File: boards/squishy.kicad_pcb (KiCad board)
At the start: 4 copper layers, 82 x 56.5 mm, 161 parts, among them J1 USB3_Micro_B_Amphenol, J2 Conn_02x26_Top_Bottom, U1 FT600Q-B-T, U10 THVD1451, U11 THVD1451, U12 THVD1451, U13 THVD1451, U14 THVD1451, U15 THVD1451, U16 THVD1451, U17 THVD1451, U18 THVD1451, U19 THVD1451, U2 ICE40HX8K-BG121, U20 THVD1451, U21 TXB0106, U22 TXB0106, U23 TXB0106, U24 TXB0106, U25 TXB0106, U26 TXB0106, U3 THVD1451, U4 THVD1451, U5 THVD1451, U6 THVD1451, U7 THVD1451, U8 THVD1451, U9 THVD1451

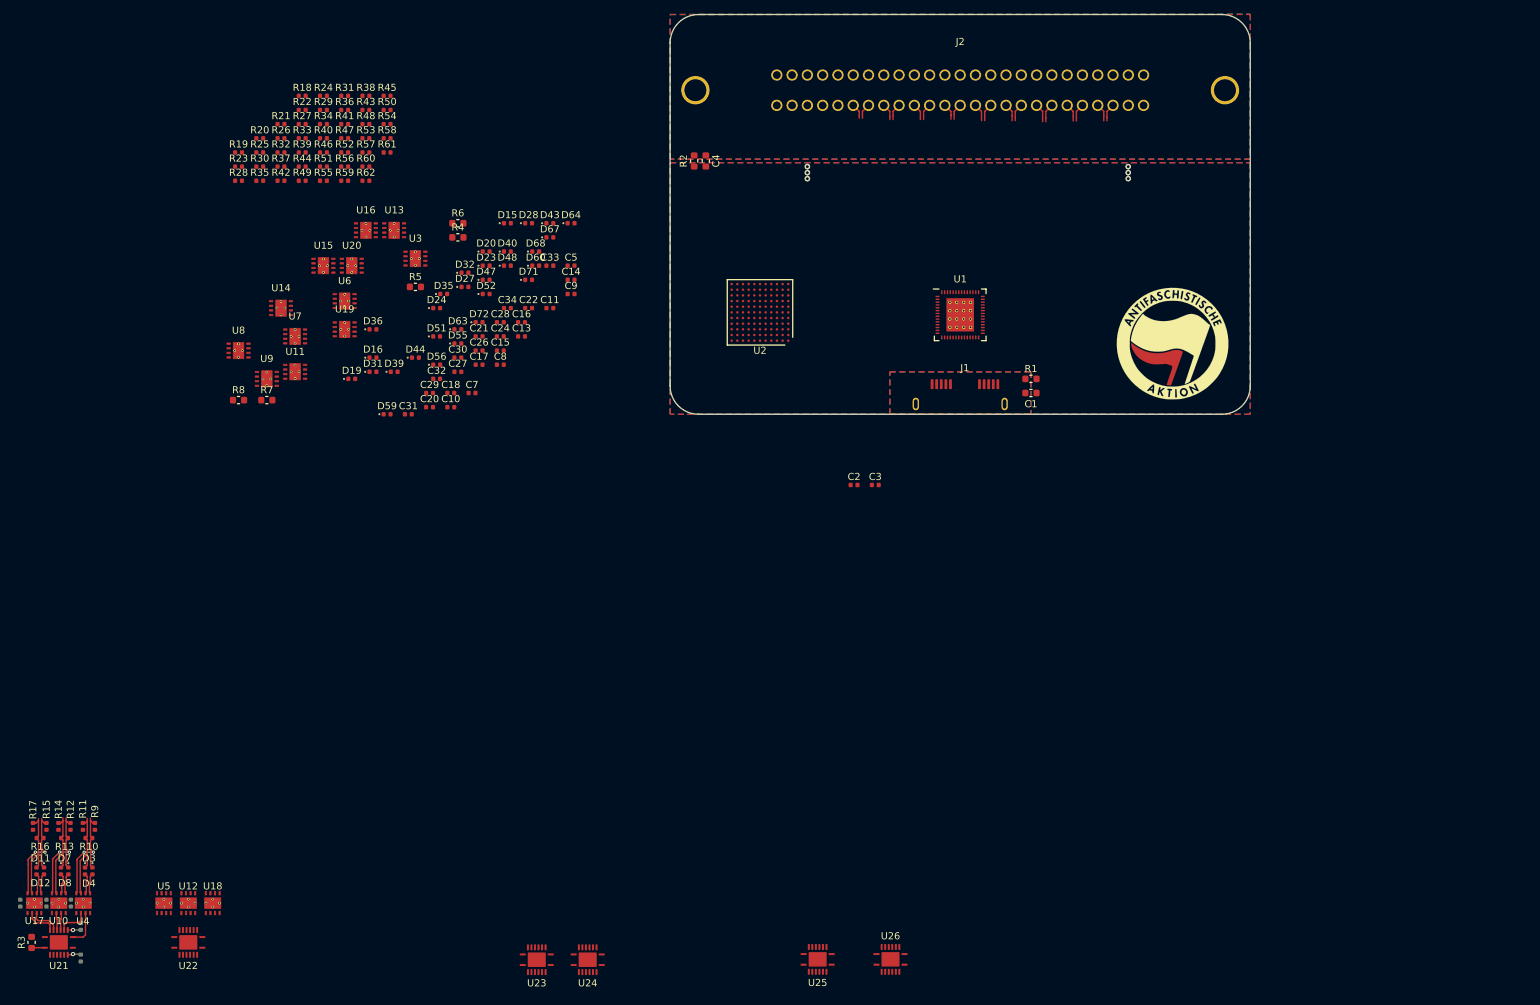
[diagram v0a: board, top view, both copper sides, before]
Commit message: Completed the layout for the faux SCSI tranciver
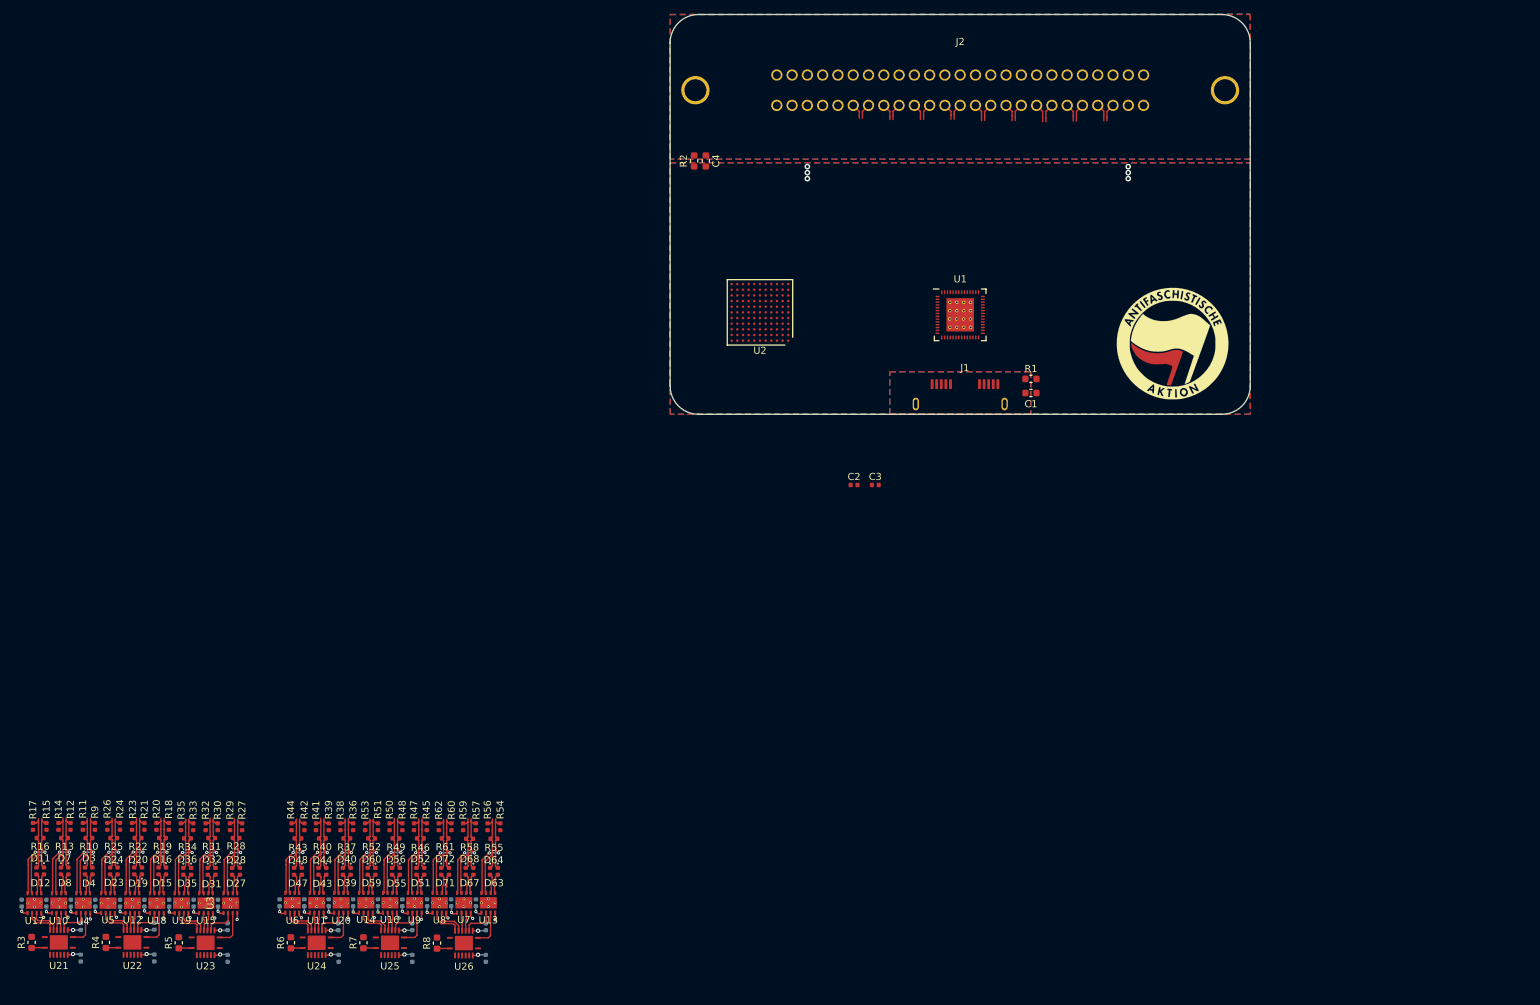
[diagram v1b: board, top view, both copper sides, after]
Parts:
- C10, C11, C13, C14, C15, C16, C17, C18, C20, C21, C22, C24, C26, C27, C28, C29, C30, C31, C32, C33, C34, C5, C7, C8, C9: moved to B.Cu
- moved R4 111.4 mm to (29.2, 174.7), turned to 90 degrees
- moved C14 108.7 mm to (31.2, 169.1), turned to 270 degrees
- moved R24 107.2 mm to (31.2, 158.2), turned to 270 degrees
- moved R31 106.6 mm to (44.2, 159.9)
- moved R22 105.5 mm to (33.8, 159.9)
- moved R18 105.0 mm to (38.1, 158.2), turned to 270 degrees
- moved R6 104.4 mm to (55.4, 174.7), turned to 90 degrees
- moved D15 104.0 mm to (36.7, 164.6), turned to 270 degrees
- moved R45 103.5 mm to (74.6, 158.3), turned to 270 degrees
- moved R43 103.4 mm to (56.4, 159.9)
- moved R38 103.4 mm to (62.4, 158.3), turned to 90 degrees
- moved C5 103.0 mm to (45.1, 169.1), turned to 270 degrees
- moved R34 102.8 mm to (40.8, 159.9)
- moved R29 102.2 mm to (46.8, 158.3), turned to 90 degrees
- moved R36 101.3 mm to (64.2, 158.3), turned to 270 degrees
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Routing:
- net +5V: track 1.85 -> 39.5 mm, vias 1 -> 24
- net Net-(D68-Pad1): track 0.00 -> 16.7 mm, vias 0 -> 2
- net Net-(D56-Pad1): track 0.00 -> 16.7 mm, vias 0 -> 2
- net Net-(D32-Pad1): track 0.00 -> 16.7 mm, vias 0 -> 2
- net Net-(D44-Pad1): track 0.00 -> 16.7 mm, vias 0 -> 2
- net Net-(D20-Pad1): track 0.00 -> 16.7 mm, vias 0 -> 2
- net Net-(D64-Pad1): track 0.00 -> 16.5 mm, vias 0 -> 2
- net Net-(D16-Pad1): track 0.00 -> 16.5 mm, vias 0 -> 2
- net Net-(D40-Pad1): track 0.00 -> 16.5 mm, vias 0 -> 2
- net Net-(D52-Pad1): track 0.00 -> 16.5 mm, vias 0 -> 2
- net Net-(D28-Pad1): track 0.00 -> 16.5 mm, vias 0 -> 2
- net Net-(D72-Pad1): track 0.00 -> 16.5 mm, vias 0 -> 2
- net Net-(D48-Pad1): track 0.00 -> 16.5 mm, vias 0 -> 2
- net Net-(D36-Pad1): track 0.00 -> 16.5 mm, vias 0 -> 2
- net Net-(D24-Pad1): track 0.00 -> 16.5 mm, vias 0 -> 2
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
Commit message: Updates, moved to an FTDI chip
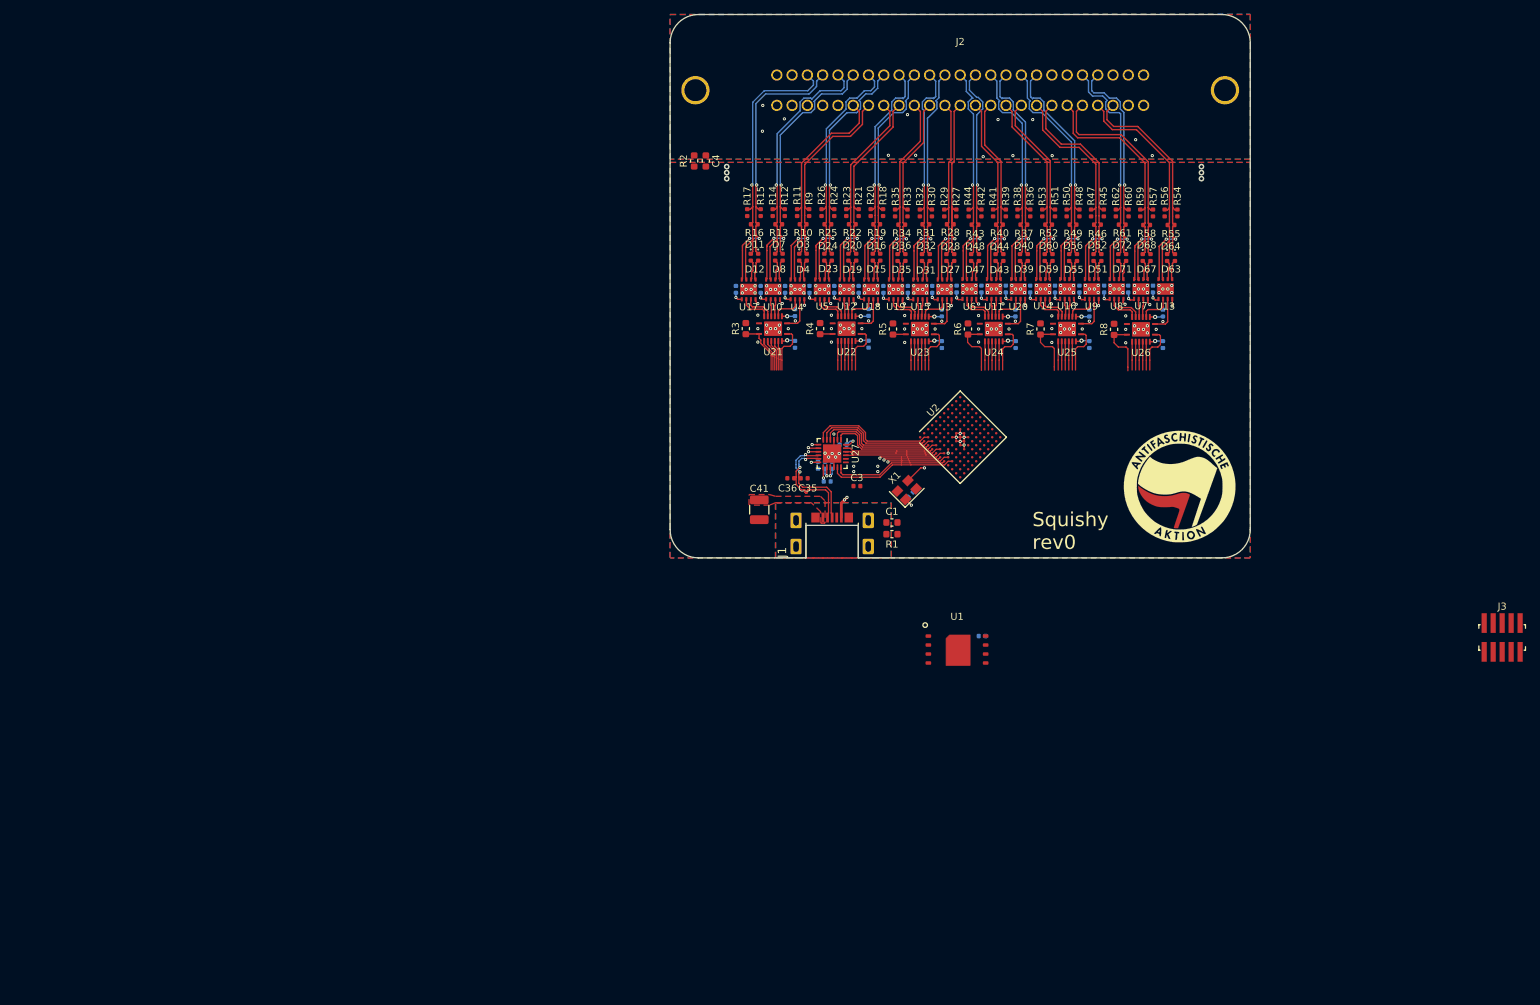
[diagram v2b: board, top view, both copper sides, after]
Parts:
- added C35: 47pf, Capacitor_SMD:C_0402_1005Metric, F.Cu at (128.0, 109.0)
- added C36: 47pf, Capacitor_SMD:C_0402_1005Metric, F.Cu at (126.0, 109.0)
- added C37: 0.1uF, Capacitor_SMD:C_0402_1005Metric, B.Cu at (131.2, 109.5)
- added C38: 0.1uF, Capacitor_SMD:C_0402_1005Metric, B.Cu at (129.9, 107.2)
- added C39: 0.1uF, Capacitor_SMD:C_0402_1005Metric, B.Cu at (131.9, 107.2)
- added C40: 0.1uF, Capacitor_SMD:C_0402_1005Metric, B.Cu at (130.9, 107.2)
- added C41: 100uF, Capacitor_SMD:C_1210_3225Metric, F.Cu at (121.6, 113.5)
- added C42: 0.1uF, Capacitor_SMD:C_0402_1005Metric, B.Cu at (133.4, 104.3)
- added C43: 0.01uF, Capacitor_SMD:C_0402_1005Metric, B.Cu at (143.0, 111.3)
- added J3: Conn_02x05_Odd_Even, lethalbit-connectors:FTSH-105-01-L-DV-K-TR, F.Cu at (226.6, 131.6)
- added U27: FT240XQ, Package_DFN_QFN:QFN-24-1EP_4x4mm_P0.5mm_EP2.6x2.6mm, F.Cu at (131.9, 105.5)
- added X1: ASEM-48MHz, Oscillator:Oscillator_SMD_Abracon_ASE-4Pin_3.2x2.5mm, F.Cu at (142.4, 110.7)
- C2: moved to B.Cu
- C3: value 0.1uF -> 0.01uF
- J1: value USB3_Micro_B_Amphenol -> USB_B_Micro; footprint lethalbit:USB3_Micro_B_Amphenol -> lethalbit-connectors:MICRO-USB-B-(IN_PCB)
- U1: value FT600Q-B-T -> 128MiB; footprint lethalbit:QFN-56_EP_7x7_Pitch0.4mm -> lethalbit-memory:WSON-8-1EP-6.0x8.0mm
- moved C23 133.1 mm to (126.7, 90.1)
- moved D11 133.1 mm to (120.4, 77.8)
- moved D12 133.1 mm to (121.5, 77.8)
- moved D15 133.1 mm to (137.7, 77.8)
- moved D3 133.1 mm to (127.2, 77.8)
- moved D8 133.1 mm to (124.9, 77.8)
- moved R29 133.1 mm to (147.8, 71.5)
- moved R30 133.1 mm to (146.0, 71.5)
- moved C20 133.1 mm to (135.7, 82.3)
- moved C21 133.1 mm to (139.2, 82.3)
- moved C24 133.1 mm to (137.1, 90.1)
- moved C25 133.1 mm to (126.7, 85.7)
- moved C26 133.1 mm to (137.1, 85.6)
- moved C27 133.1 mm to (147.4, 90.2)
- moved C29 133.1 mm to (147.4, 85.7)
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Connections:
- net Net-(R5-Pad1) renamed /BNK2_OE
- net Net-(R6-Pad1) renamed /BNK3_OE
- net Net-(U2-PadC11) renamed /MSG_RX
- net Net-(U2-PadD10) renamed /MSG_TX
- net Net-(U2-PadD11) renamed /DB5_RX
- net Net-(U2-PadD4) renamed +1V2
- net Net-(U2-PadD9) renamed /SEL_RX
- net Net-(U2-PadE11) renamed /DB5_TX
- net Net-(U2-PadE8) renamed /SEL_TX
- net Net-(U2-PadG8) renamed /DB3_TX
- net Net-(U2-PadH10) renamed /RST_TX
- net Net-(U2-PadH11) renamed /DB3_RX
- net Net-(U2-PadJ10) renamed /RST_RX
- net Net-(U2-PadJ11) renamed /DB4_TX
- net Net-(U2-PadK11) renamed /DB4_RX
- C1 pad 1: Net-(C1-Pad1) -> GND
- C1 pad 2: GND -> Net-(C1-Pad2)
- C2 pad 1: Net-(C2-Pad1) -> GND
- C2 pad 2: Net-(C2-Pad2) -> +3V3
- C3 pad 1: Net-(C3-Pad1) -> +5V
- C3 pad 2: Net-(C3-Pad2) -> GND
- D11 pad 1: /_2- -> /IO-
- D12 pad 1: /_2+ -> /IO+
- D15 pad 1: Net-(D15-Pad1) -> /SEL-
- D16 pad 1: Net-(D16-Pad1) -> /SEL+
- D19 pad 1: Net-(D19-Pad1) -> /DB7-
- D20 pad 1: Net-(D20-Pad1) -> /DB7+
- D23 pad 1: Net-(D23-Pad1) -> /CD-
- D24 pad 1: Net-(D24-Pad1) -> /CD+
- D27 pad 1: Net-(D27-Pad1) -> /DB5-
- D28 pad 1: Net-(D28-Pad1) -> /DB5+
- D3 pad 1: /_0- -> /DBP-
- D31 pad 1: Net-(D31-Pad1) -> /MSG-
- D32 pad 1: Net-(D32-Pad1) -> /MSG+
- D35 pad 1: Net-(D35-Pad1) -> /DB6-
- D36 pad 1: Net-(D36-Pad1) -> /DB6+
- D39 pad 1: Net-(D39-Pad1) -> /ACK-
- D4 pad 1: /_0+ -> /DBP+
- D40 pad 1: Net-(D40-Pad1) -> /ACK+
- D43 pad 1: Net-(D43-Pad1) -> /DB4-
- D44 pad 1: Net-(D44-Pad1) -> /DB4+
- D47 pad 1: Net-(D47-Pad1) -> /RST-
- D48 pad 1: Net-(D48-Pad1) -> /RST+
- D51 pad 1: Net-(D51-Pad1) -> /DB2-
- D52 pad 1: Net-(D52-Pad1) -> /DB2+
- D55 pad 1: Net-(D55-Pad1) -> /BSY-
- D56 pad 1: Net-(D56-Pad1) -> /BSY+
- D59 pad 1: Net-(D59-Pad1) -> /DB3-
- D60 pad 1: Net-(D60-Pad1) -> /DB3+
- D63 pad 1: Net-(D63-Pad1) -> /DB0-
- D64 pad 1: Net-(D64-Pad1) -> /DB0+
- D67 pad 1: Net-(D67-Pad1) -> /DB1-
- D68 pad 1: Net-(D68-Pad1) -> /DB1+
- D7 pad 1: /_1- -> /REQ-
- D71 pad 1: Net-(D71-Pad1) -> /ATN-
- D72 pad 1: Net-(D72-Pad1) -> /ATN+
- D8 pad 1: /_1+ -> /REQ+
- J1 pad 2: Net-(J1-Pad2) -> /D-
- J1 pad 3: Net-(J1-Pad3) -> /D+
- J1 pad 4: Net-(J1-Pad4) -> +5V
- J1 pad 6: Net-(J1-Pad6) -> Net-(C1-Pad2)
- R1 pad 1: Net-(C1-Pad1) -> GND
- R1 pad 2: GND -> Net-(C1-Pad2)
- R10 pad 1: /_0- -> /DBP-
- R10 pad 2: /_0+ -> /DBP+
- R11 pad 2: /_0- -> /DBP-
- R12 pad 1: /_1+ -> /REQ+
- R13 pad 1: /_1- -> /REQ-
- R13 pad 2: /_1+ -> /REQ+
- R14 pad 2: /_1- -> /REQ-
- R15 pad 1: /_2+ -> /IO+
- R16 pad 1: /_2- -> /IO-
- R16 pad 2: /_2+ -> /IO+
- R17 pad 2: /_2- -> /IO-
- R18 pad 1: Net-(D16-Pad1) -> /SEL+
- R19 pad 1: Net-(D15-Pad1) -> /SEL-
- R19 pad 2: Net-(D16-Pad1) -> /SEL+
- R20 pad 2: Net-(D15-Pad1) -> /SEL-
- R21 pad 1: Net-(D20-Pad1) -> /DB7+
- R22 pad 1: Net-(D19-Pad1) -> /DB7-
- R22 pad 2: Net-(D20-Pad1) -> /DB7+
- R23 pad 2: Net-(D19-Pad1) -> /DB7-
- R24 pad 1: Net-(D24-Pad1) -> /CD+
- R25 pad 1: Net-(D23-Pad1) -> /CD-
- R25 pad 2: Net-(D24-Pad1) -> /CD+
- R26 pad 2: Net-(D23-Pad1) -> /CD-
- R27 pad 1: Net-(D28-Pad1) -> /DB5+
- R28 pad 1: Net-(D27-Pad1) -> /DB5-
- R28 pad 2: Net-(D28-Pad1) -> /DB5+
- R29 pad 2: Net-(D27-Pad1) -> /DB5-
- R3 pad 1: Net-(R3-Pad1) -> /BNK0_OE
- R30 pad 1: Net-(D32-Pad1) -> /MSG+
- R31 pad 1: Net-(D31-Pad1) -> /MSG-
- R31 pad 2: Net-(D32-Pad1) -> /MSG+
- R32 pad 2: Net-(D31-Pad1) -> /MSG-
- R33 pad 1: Net-(D36-Pad1) -> /DB6+
- R34 pad 1: Net-(D35-Pad1) -> /DB6-
- R34 pad 2: Net-(D36-Pad1) -> /DB6+
- R35 pad 2: Net-(D35-Pad1) -> /DB6-
- R36 pad 1: Net-(D40-Pad1) -> /ACK+
- R37 pad 1: Net-(D39-Pad1) -> /ACK-
- R37 pad 2: Net-(D40-Pad1) -> /ACK+
- R38 pad 2: Net-(D39-Pad1) -> /ACK-
- R39 pad 1: Net-(D44-Pad1) -> /DB4+
- R4 pad 1: Net-(R4-Pad1) -> /BNK1_OE
- R40 pad 1: Net-(D43-Pad1) -> /DB4-
- R40 pad 2: Net-(D44-Pad1) -> /DB4+
- R41 pad 2: Net-(D43-Pad1) -> /DB4-
- R42 pad 1: Net-(D48-Pad1) -> /RST+
- R43 pad 1: Net-(D47-Pad1) -> /RST-
- R43 pad 2: Net-(D48-Pad1) -> /RST+
- R44 pad 2: Net-(D47-Pad1) -> /RST-
- R45 pad 1: Net-(D52-Pad1) -> /DB2+
- R46 pad 1: Net-(D51-Pad1) -> /DB2-
- R46 pad 2: Net-(D52-Pad1) -> /DB2+
- R47 pad 2: Net-(D51-Pad1) -> /DB2-
- R48 pad 1: Net-(D56-Pad1) -> /BSY+
- R49 pad 1: Net-(D55-Pad1) -> /BSY-
- R49 pad 2: Net-(D56-Pad1) -> /BSY+
- R50 pad 2: Net-(D55-Pad1) -> /BSY-
- R51 pad 1: Net-(D60-Pad1) -> /DB3+
- R52 pad 1: Net-(D59-Pad1) -> /DB3-
- R52 pad 2: Net-(D60-Pad1) -> /DB3+
- R53 pad 2: Net-(D59-Pad1) -> /DB3-
- R54 pad 1: Net-(D64-Pad1) -> /DB0+
- R55 pad 1: Net-(D63-Pad1) -> /DB0-
- R55 pad 2: Net-(D64-Pad1) -> /DB0+
- R56 pad 2: Net-(D63-Pad1) -> /DB0-
- R57 pad 1: Net-(D68-Pad1) -> /DB1+
- R58 pad 1: Net-(D67-Pad1) -> /DB1-
- R58 pad 2: Net-(D68-Pad1) -> /DB1+
- R59 pad 2: Net-(D67-Pad1) -> /DB1-
- R60 pad 1: Net-(D72-Pad1) -> /ATN+
- R61 pad 1: Net-(D71-Pad1) -> /ATN-
- R61 pad 2: Net-(D72-Pad1) -> /ATN+
- R62 pad 2: Net-(D71-Pad1) -> /ATN-
- R7 pad 1: Net-(R7-Pad1) -> /BNK4_OE
- R8 pad 1: Net-(R8-Pad1) -> /BNK5_OE
- R9 pad 1: /_0+ -> /DBP+
- U1 pad 4: Net-(U1-Pad4) -> GND
- U1 pad 8: Net-(U1-Pad8) -> +3V3
- U1 pad 9: Net-(U1-Pad9) -> GND
- U10 pad 7: /_1- -> /REQ-
- U10 pad 8: /_1+ -> /REQ+
- U11 pad 7: Net-(D43-Pad1) -> /DB4-
- U11 pad 8: Net-(D44-Pad1) -> /DB4+
- U12 pad 7: Net-(D19-Pad1) -> /DB7-
- U12 pad 8: Net-(D20-Pad1) -> /DB7+
- U13 pad 7: Net-(D63-Pad1) -> /DB0-
- U13 pad 8: Net-(D64-Pad1) -> /DB0+
- U14 pad 7: Net-(D59-Pad1) -> /DB3-
- U14 pad 8: Net-(D60-Pad1) -> /DB3+
- U15 pad 7: Net-(D31-Pad1) -> /MSG-
- U15 pad 8: Net-(D32-Pad1) -> /MSG+
- U16 pad 7: Net-(D55-Pad1) -> /BSY-
- U16 pad 8: Net-(D56-Pad1) -> /BSY+
- U17 pad 7: /_2- -> /IO-
- U17 pad 8: /_2+ -> /IO+
- U18 pad 7: Net-(D15-Pad1) -> /SEL-
- U18 pad 8: Net-(D16-Pad1) -> /SEL+
- U19 pad 7: Net-(D35-Pad1) -> /DB6-
- U19 pad 8: Net-(D36-Pad1) -> /DB6+
- U2 pad A1: Net-(R4-Pad1) -> /DB1_TX
- U2 pad A10: Net-(U2-PadA10) -> /BSY_RX
- U2 pad A11: Net-(U2-PadA11) -> /BNK1_OE
- U2 pad A2: Net-(U2-PadA2) -> /ATN_TX
- U2 pad A3: Net-(U2-PadA3) -> /DB1_RX
- U2 pad A4: Net-(U2-PadA4) -> /BNK0_OE
- U2 pad A5: Net-(U2-PadA5) -> /IO_RX
- U2 pad A6: Net-(U2-PadA6) -> /DBP_TX
- U2 pad A7: Net-(U2-PadA7) -> /REQ_RX
- U2 pad A9: Net-(U2-PadA9) -> /ACK_RX
- U2 pad B1: Net-(U2-PadB1) -> /D6
- U2 pad B2: Net-(U2-PadB2) -> /D3
- U2 pad B3: Net-(U2-PadB3) -> /ATN_RX
- U2 pad B4: Net-(U2-PadB4) -> /DB0_TX
- U2 pad B5: Net-(U2-PadB5) -> /IO_TX
- U2 pad B6: Net-(U2-PadB6) -> /DBP_RX
- U2 pad B7: Net-(U2-PadB7) -> /REQ_TX
- U2 pad B8: Net-(U2-PadB8) -> /DB2_TX
- U2 pad B9: Net-(U2-PadB9) -> /DB2_RX
- U2 pad C1: Net-(U2-PadC1) -> /D7
- U2 pad C10: Net-(U2-PadC10) -> +3V3
- U2 pad C2: Net-(U2-PadC2) -> /D5
- U2 pad C7: Net-(U2-PadC7) -> /BNK5_OE
- U2 pad C8: Net-(R3-Pad1) -> /ACK_TX
- U2 pad C9: Net-(U2-PadC9) -> /BSY_TX
- U2 pad D1: Net-(U2-PadD1) -> /D2
- U2 pad D2: Net-(U2-PadD2) -> /D1
- U2 pad D3: Net-(R7-Pad1) -> Net-(U2-PadD3)
- U2 pad D5: Net-(U2-PadD5) -> /DB0_RX
- U2 pad E1: Net-(U2-PadE1) -> /D0
- U2 pad E10: Net-(U2-PadE10) -> /DB6_RX
- U2 pad E2: Net-(U2-PadE2) -> /D4
- U2 pad E5: Net-(U2-PadE5) -> GND
- U2 pad E6: Net-(U2-PadE5) -> GND
- U2 pad E7: Net-(U2-PadE5) -> GND
- U2 pad E9: Net-(U2-PadE9) -> /BNK4_OE
- U2 pad F1: Net-(U2-PadF1) -> /~RD
- U2 pad F10: Net-(U2-PadF10) -> /CD_TX
- U2 pad F11: Net-(U2-PadF11) -> /DB6_TX
- U2 pad F2: Net-(U2-PadF2) -> /~SI_WU
- U2 pad F3: Net-(U2-PadF3) -> /GLOBAL_CLK
- U2 pad F5: Net-(U2-PadE5) -> GND
- U2 pad F6: Net-(U2-PadE5) -> GND
- U2 pad F7: Net-(U2-PadE5) -> GND
- U2 pad F9: Net-(U2-PadF9) -> /CD_RX
- U2 pad G1: Net-(U2-PadG1) -> /~RXF
- U2 pad G11: Net-(U2-PadG11) -> /DB7_RX
- U2 pad G2: Net-(U2-PadG2) -> /~WR
- U2 pad G5: Net-(U2-PadE5) -> GND
- U2 pad G6: Net-(U2-PadE5) -> GND
- U2 pad G7: Net-(U2-PadE5) -> GND
- U2 pad G9: Net-(U2-PadG9) -> /DB7_TX
- U2 pad H2: Net-(U2-PadH2) -> /~TXF
- U2 pad H5: Net-(U2-PadE5) -> GND
- U2 pad H6: Net-(U2-PadH6) -> +3V3
- U2 pad J2: Net-(R8-Pad1) -> Net-(U2-PadJ2)
- U2 pad J9: Net-(U2-PadJ9) -> Net-(U1-Pad2)
- U2 pad K10: Net-(U2-PadK10) -> Net-(U1-Pad1)
- U2 pad K9: Net-(U2-PadK9) -> Net-(U1-Pad5)
- U2 pad L10: Net-(U2-PadL10) -> Net-(U1-Pad6)
- U2 pad L11: Net-(U2-PadL11) -> +3V3
- U20 pad 7: Net-(D39-Pad1) -> /ACK-
- U20 pad 8: Net-(D40-Pad1) -> /ACK+
- U21 pad 1: Net-(U2-PadA11) -> /DB1_TX
- U21 pad 3: Net-(U2-PadA10) -> /DB1_RX
- U21 pad 4: Net-(U2-PadC9) -> /ATN_TX
- U21 pad 5: Net-(U2-PadB9) -> /ATN_RX
- U21 pad 6: Net-(U2-PadB8) -> /DB0_TX
- U21 pad 7: Net-(U2-PadA9) -> /DB0_RX
- U21 pad 8: Net-(R3-Pad1) -> /BNK0_OE
- U22 pad 1: Net-(U2-PadA4) -> /ACK_TX
- U22 pad 3: Net-(U2-PadD5) -> /ACK_RX
- U22 pad 4: Net-(U2-PadB4) -> /DB2_TX
- U22 pad 5: Net-(U2-PadB3) -> /DB2_RX
- U22 pad 6: Net-(U2-PadA2) -> /BSY_TX
- U22 pad 7: Net-(U2-PadA3) -> /BSY_RX
- U22 pad 8: Net-(R4-Pad1) -> /BNK1_OE
- U25 pad 1: Net-(U2-PadC3) -> /DB7_TX
- U25 pad 3: Net-(U2-PadC2) -> /DB7_RX
- U25 pad 4: Net-(U2-PadC1) -> /CD_TX
- U25 pad 5: Net-(U2-PadE1) -> /CD_RX
- U25 pad 6: Net-(U2-PadD1) -> /DB6_TX
- U25 pad 7: Net-(U2-PadD2) -> /DB6_RX
- U25 pad 8: Net-(R7-Pad1) -> /BNK4_OE
- U26 pad 1: Net-(U2-PadH3) -> /IO_TX
- U26 pad 3: Net-(U2-PadH1) -> /IO_RX
- U26 pad 4: Net-(U2-PadH2) -> /DBP_TX
- U26 pad 5: Net-(U2-PadJ1) -> /DBP_RX
- U26 pad 6: Net-(U2-PadK1) -> /REQ_TX
- U26 pad 7: Net-(U2-PadK2) -> /REQ_RX
- U26 pad 8: Net-(R8-Pad1) -> /BNK5_OE
- U3 pad 7: Net-(D27-Pad1) -> /DB5-
- U3 pad 8: Net-(D28-Pad1) -> /DB5+
- U4 pad 7: /_0- -> /DBP-
- U4 pad 8: /_0+ -> /DBP+
- U5 pad 7: Net-(D23-Pad1) -> /CD-
- U5 pad 8: Net-(D24-Pad1) -> /CD+
- U6 pad 7: Net-(D47-Pad1) -> /RST-
- U6 pad 8: Net-(D48-Pad1) -> /RST+
- U7 pad 7: Net-(D67-Pad1) -> /DB1-
- U7 pad 8: Net-(D68-Pad1) -> /DB1+
- U8 pad 7: Net-(D71-Pad1) -> /ATN-
- U8 pad 8: Net-(D72-Pad1) -> /ATN+
- U9 pad 7: Net-(D51-Pad1) -> /DB2-
- U9 pad 8: Net-(D52-Pad1) -> /DB2+
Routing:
- net GND: track 65.4 -> 108.9 mm, vias 24 -> 215
- net /IO+: track 0.00 -> 42.4 mm, vias 0 -> 3
- net /REQ+: track 0.00 -> 41.7 mm, vias 0 -> 3
- net /IO-: track 0.00 -> 40.3 mm, vias 0 -> 1
- net /CD+: track 0.00 -> 39.6 mm, vias 0 -> 3
- net /REQ-: track 0.00 -> 39.3 mm, vias 0 -> 1
- net /BSY+: track 0.00 -> 38.7 mm, vias 0 -> 3
- net /ATN+: track 0.00 -> 38.7 mm, vias 0 -> 3
- net /SEL+: track 0.00 -> 37.9 mm, vias 0 -> 3
- net /ACK+: track 0.00 -> 37.5 mm, vias 0 -> 3
- net /CD-: track 0.00 -> 37.1 mm, vias 0 -> 1
- net /ATN-: track 0.00 -> 37.0 mm, vias 0 -> 1
- net /RST+: track 0.00 -> 36.6 mm, vias 0 -> 3
- net /BSY-: track 0.00 -> 36.3 mm, vias 0 -> 1
- net /MSG+: track 0.00 -> 36.2 mm, vias 0 -> 3
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- added copper zone on F.Cu, net +5V
- added copper zone on B.Cu, net Net-(C1-Pad2)
- added copper zone on F.Cu, net Net-(C1-Pad2)
- added copper zone on In1.Cu, net Net-(C1-Pad2)
- added copper zone on In2.Cu, net Net-(C1-Pad2)
- removed copper zone on B.Cu, net Net-(C1-Pad1)
- removed copper zone on F.Cu, net Net-(C1-Pad1)
- removed copper zone on In1.Cu, net Net-(C1-Pad1)
- removed copper zone on In2.Cu, net Net-(C1-Pad1)
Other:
- board size 82 x 56.5 mm -> 82 x 76.8 mm
- board text added: "Squishy rev0"
